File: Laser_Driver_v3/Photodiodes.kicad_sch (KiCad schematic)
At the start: 11 parts, among them U43 LT3042EMSE +12V

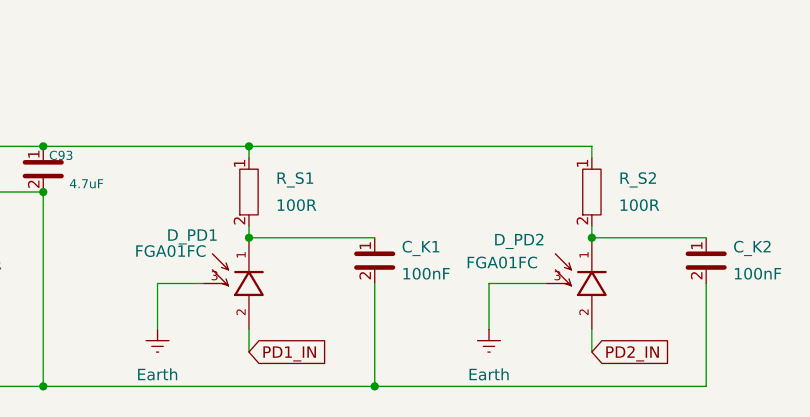
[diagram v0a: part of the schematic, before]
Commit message: Split into a power and signal board.
I think all footprints are now valid.  Need to figure out the power connections between boards, currently just screw terminals for wire.  I think a single multi-pin connector will work, but want to find something with premade off the shelf cables.
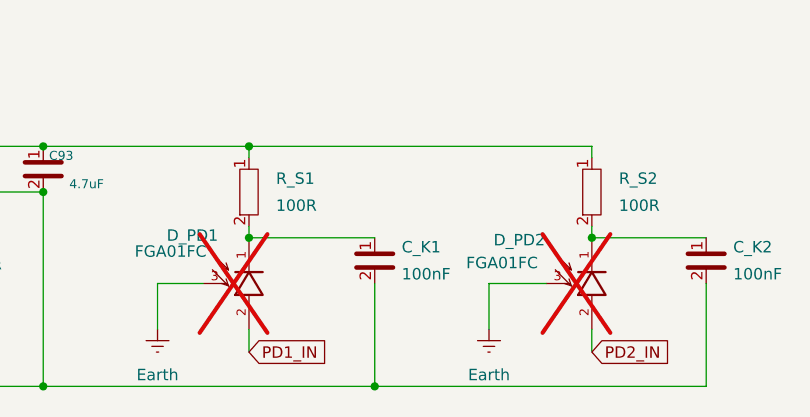
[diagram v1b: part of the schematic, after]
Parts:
- D_PD1, D_PD2: now not fitted
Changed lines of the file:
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@@
 		(unit 1)
 		(body_style 1)
-		(exclude_from_sim no)
-		(in_bom yes)
-		(on_board yes)
-		(in_pos_files yes)
-		(dnp no)
+		(exclude_from_sim yes)
+		(in_bom yes)
+		(on_board no)
+		(in_pos_files yes)
+		(dnp yes)
 		(property "Reference" "D_PD1"
 			(at 94.996 84.836 0)
@@
 		(unit 1)
 		(body_style 1)
-		(exclude_from_sim no)
-		(in_bom yes)
-		(on_board yes)
-		(in_pos_files yes)
-		(dnp no)
+		(exclude_from_sim yes)
+		(in_bom yes)
+		(on_board no)
+		(in_pos_files yes)
+		(dnp yes)
 		(property "Reference" "D_PD2"
 			(at 131.318 85.344 0)

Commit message: Fixed board after update and crash
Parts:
- renumbered C92 to C1, C93 to C2, R114 to R1, R115 to R2, U43 to U1
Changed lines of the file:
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@@
 		(in_pos_files yes)
 		(dnp no)
-		(property "Reference" "U43"
+		(property "Reference" "U1"
 			(at 46.99 72.39 0)
 			(show_name no)
@@
 		(instances
 			(project "laser_driver_v3"
-				(path "/b2c3d4e5-f6a7-8901-bcde-f12345678901/5a800bdf-c78b-4bfb-a7c6-d84c2550e565"
-					(reference "U43")
+				(path "/b2c3d4e5-f6a7-8901-bcde-f12345678901/633e8ae1-9acc-41a6-b8dc-30d28641fade"
+					(reference "U1")
 					(unit 1)
 				)
@@
 		(in_pos_files yes)
 		(dnp no)
-		(property "Reference" "C92"
+		(property "Reference" "C1"
 			(at 70.612 84.582 0)
 			(show_name no)
@@
 		(instances
 			(project "laser_driver_v3"
-				(path "/b2c3d4e5-f6a7-8901-bcde-f12345678901/5a800bdf-c78b-4bfb-a7c6-d84c2550e565"
-					(reference "C92")
+				(path "/b2c3d4e5-f6a7-8901-bcde-f12345678901/633e8ae1-9acc-41a6-b8dc-30d28641fade"
+					(reference "C1")
 					(unit 1)
 				)
@@
 		(in_pos_files yes)
 		(dnp no)
-		(property "Reference" "C93"
+		(property "Reference" "C2"
 			(at 83.28 75.97 0)
 			(show_name no)
@@
 		(instances
 			(project "laser_driver_v3"
-				(path "/b2c3d4e5-f6a7-8901-bcde-f12345678901/5a800bdf-c78b-4bfb-a7c6-d84c2550e565"
-					(reference "C93")
+				(path "/b2c3d4e5-f6a7-8901-bcde-f12345678901/633e8ae1-9acc-41a6-b8dc-30d28641fade"
+					(reference "C2")
 					(unit 1)
 				)
@@
 		(in_pos_files yes)
 		(dnp no)
-		(property "Reference" "R114"
+		(property "Reference" "R1"
 			(at 37.56 91.21 0)
 			(show_name no)
@@
 		(instances
 			(project "laser_driver_v3"
-				(path "/b2c3d4e5-f6a7-8901-bcde-f12345678901/5a800bdf-c78b-4bfb-a7c6-d84c2550e565"
-					(reference "R114")
+				(path "/b2c3d4e5-f6a7-8901-bcde-f12345678901/633e8ae1-9acc-41a6-b8dc-30d28641fade"
+					(reference "R1")
 					(unit 1)
 				)
@@
 		(instances
 			(project "laser_driver_v3"
-				(path "/b2c3d4e5-f6a7-8901-bcde-f12345678901/5a800bdf-c78b-4bfb-a7c6-d84c2550e565"
+				(path "/b2c3d4e5-f6a7-8901-bcde-f12345678901/633e8ae1-9acc-41a6-b8dc-30d28641fade"
 					(reference "#PWR026")
 					(unit 1)
@@
 		(in_pos_files yes)
 		(dnp no)
-		(property "Reference" "R115"
+		(property "Reference" "R2"
 			(at 60.42 84.86 0)
 			(show_name no)
@@
 		(instances
 			(project "laser_driver_v3"
-				(path "/b2c3d4e5-f6a7-8901-bcde-f12345678901/5a800bdf-c78b-4bfb-a7c6-d84c2550e565"
-					(reference "R115")
+				(path "/b2c3d4e5-f6a7-8901-bcde-f12345678901/633e8ae1-9acc-41a6-b8dc-30d28641fade"
+					(reference "R2")
 					(unit 1)
 				)
@@
 		(instances
 			(project "laser_driver_v3"
-				(path "/b2c3d4e5-f6a7-8901-bcde-f12345678901/5a800bdf-c78b-4bfb-a7c6-d84c2550e565"
+				(path "/b2c3d4e5-f6a7-8901-bcde-f12345678901/633e8ae1-9acc-41a6-b8dc-30d28641fade"
 					(reference "R_S1")
 					(unit 1)
@@
 		(instances
 			(project "laser_driver_v3"
-				(path "/b2c3d4e5-f6a7-8901-bcde-f12345678901/5a800bdf-c78b-4bfb-a7c6-d84c2550e565"
+				(path "/b2c3d4e5-f6a7-8901-bcde-f12345678901/633e8ae1-9acc-41a6-b8dc-30d28641fade"
 					(reference "D_PD1")
 					(unit 1)
@@
 		(instances
 			(project "laser_driver_v3"
-				(path "/b2c3d4e5-f6a7-8901-bcde-f12345678901/5a800bdf-c78b-4bfb-a7c6-d84c2550e565"
+				(path "/b2c3d4e5-f6a7-8901-bcde-f12345678901/633e8ae1-9acc-41a6-b8dc-30d28641fade"
 					(reference "C_K1")
 					(unit 1)
@@
 		(instances
 			(project "laser_driver_v3"
-				(path "/b2c3d4e5-f6a7-8901-bcde-f12345678901/5a800bdf-c78b-4bfb-a7c6-d84c2550e565"
+				(path "/b2c3d4e5-f6a7-8901-bcde-f12345678901/633e8ae1-9acc-41a6-b8dc-30d28641fade"
 					(reference "R_S2")
 					(unit 1)
@@
 		(instances
 			(project "laser_driver_v3"
-				(path "/b2c3d4e5-f6a7-8901-bcde-f12345678901/5a800bdf-c78b-4bfb-a7c6-d84c2550e565"
+				(path "/b2c3d4e5-f6a7-8901-bcde-f12345678901/633e8ae1-9acc-41a6-b8dc-30d28641fade"
 					(reference "D_PD2")
 					(unit 1)
@@
 		(instances
 			(project "laser_driver_v3"
-				(path "/b2c3d4e5-f6a7-8901-bcde-f12345678901/5a800bdf-c78b-4bfb-a7c6-d84c2550e565"
+				(path "/b2c3d4e5-f6a7-8901-bcde-f12345678901/633e8ae1-9acc-41a6-b8dc-30d28641fade"
 					(reference "C_K2")
 					(unit 1)
@@
 		(instances
 			(project "laser_driver_v3"
-				(path "/b2c3d4e5-f6a7-8901-bcde-f12345678901/5a800bdf-c78b-4bfb-a7c6-d84c2550e565"
+				(path "/b2c3d4e5-f6a7-8901-bcde-f12345678901/633e8ae1-9acc-41a6-b8dc-30d28641fade"
 					(reference "#PWR027")
 					(unit 1)
@@
 		)
 	)
-	(sheet_instances
-		(path "/"
-			(page "17")
-		)
-	)
